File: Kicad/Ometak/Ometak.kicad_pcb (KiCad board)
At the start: 2 copper layers, 49.3 x 41 mm, 24 parts, among them J1 Conn_01x02_Pin, J2 Conn_01x02_Pin, J3 Conn_01x02_Pin, Q1 IRF7303, U1 L7805, U2 PIC16F15214-I/SN, U3 LM358

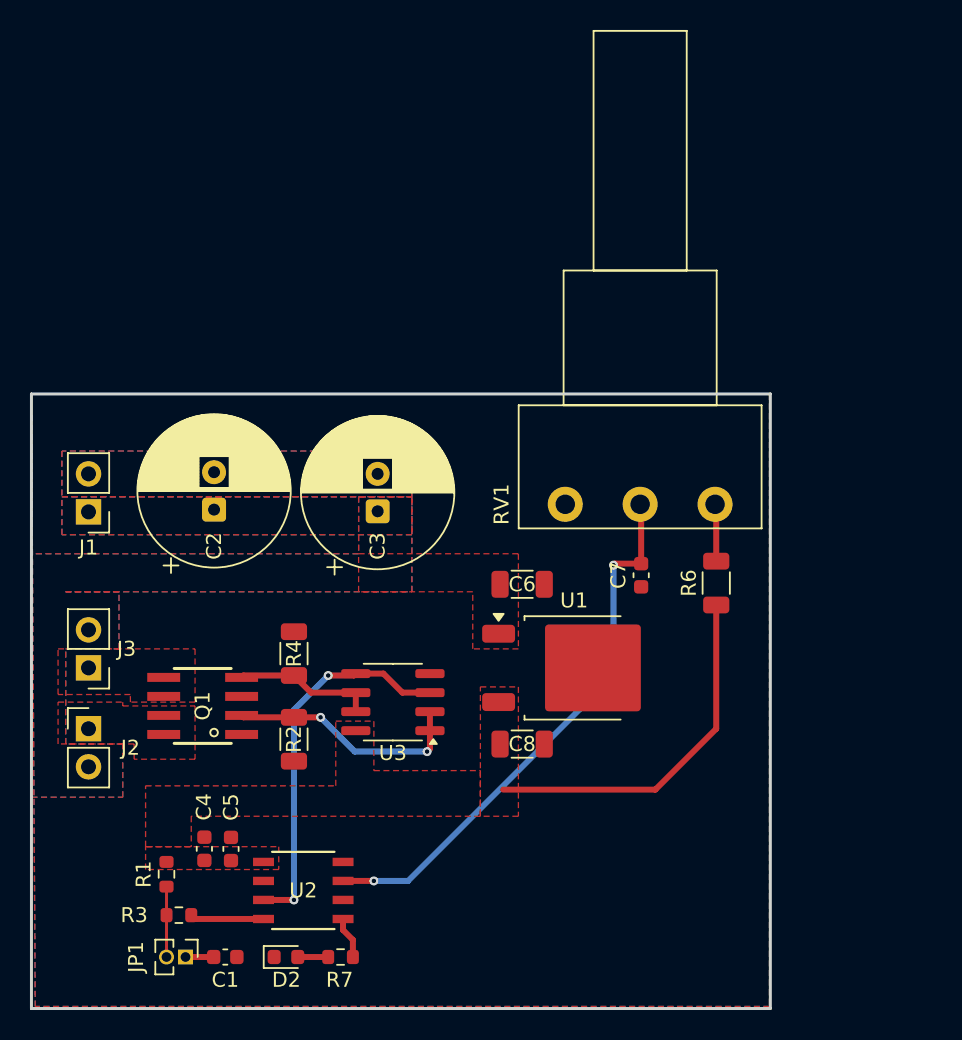
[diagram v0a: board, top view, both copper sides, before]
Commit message: Pokrocilejsi verze ometaku - navrh
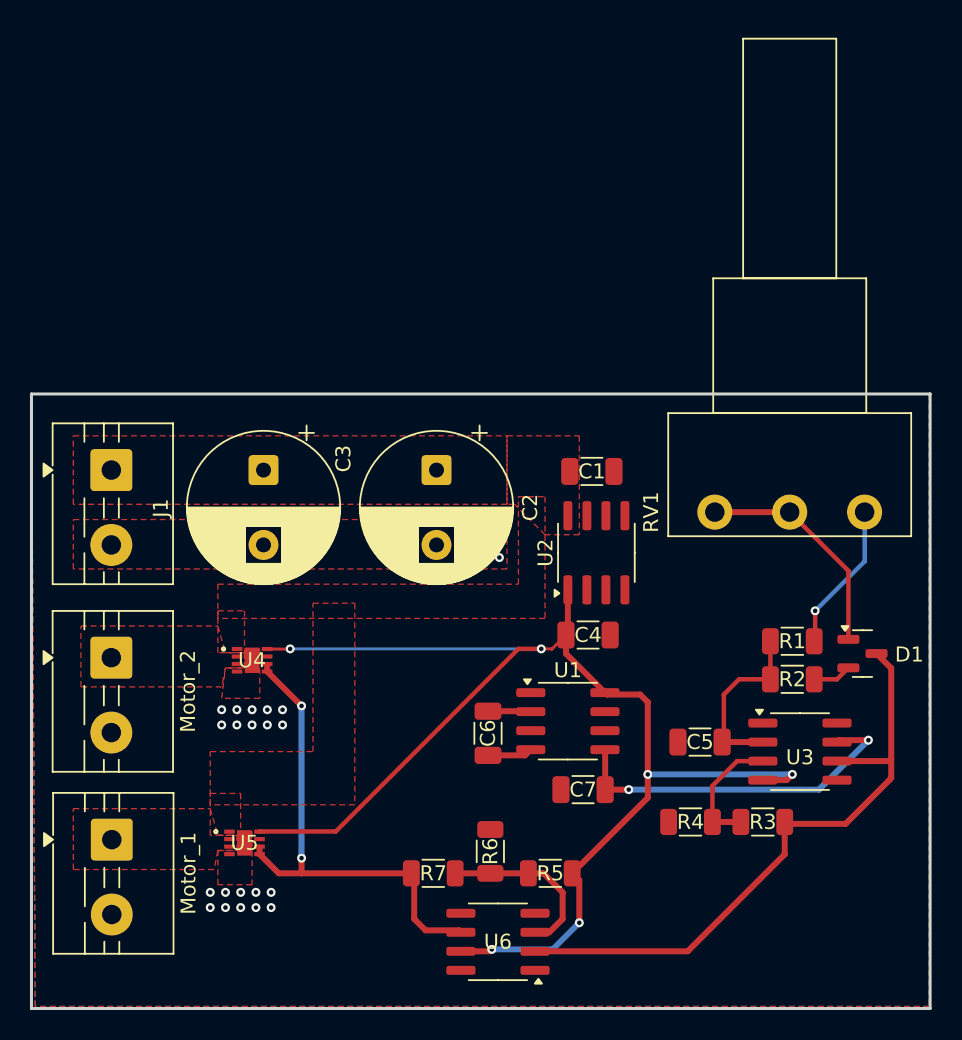
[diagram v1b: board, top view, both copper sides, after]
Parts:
- removed C8: 0.1u, Capacitor_SMD:C_1206_3216Metric
- removed D2: LED, LED_SMD:LED_0603_1608Metric
- removed J2, J3: Conn_01x02_Pin, Connector_PinHeader_2.54mm:PinHeader_1x02_P2.54mm_Vertical
- removed JP1: Jumper_2_Open, Connector_PinHeader_1.27mm:PinHeader_1x02_P1.27mm_Vertical
- removed Q1: IRF7303, IRF7303:SOIC-8
- added D1: BAS40-04, Package_TO_SOT_SMD:SOT-23, F.Cu at (132.4, 89.5)
- added Motor_1: Conn_01x02_Pin, TerminalBlock:TerminalBlock_MaiXu_MX126-5.0-02P_1x02_P5.00mm, F.Cu at (82.3, 101.9)
- added Motor_2: Conn_01x02_Pin, TerminalBlock:TerminalBlock_MaiXu_MX126-5.0-02P_1x02_P5.00mm, F.Cu at (82.3, 89.7)
- added R5: R, Resistor_SMD:R_1206_3216Metric, F.Cu at (111.6, 104.1)
- added U4: DRV8220DSGR, DRV8220:WSON8_DSG_TEX, F.Cu at (91.7, 89.9)
- added U5: DRV8220DSGR, DRV8220:WSON8_DSG_TEX, F.Cu at (91.2, 102.1)
- added U6: OPA333xxD, Package_SO:SOIC-8_3.9x4.9mm_P1.27mm, F.Cu at (108.1, 108.7)
- C1: value C -> 0.33 uF; footprint Capacitor_SMD:C_0603_1608Metric -> Capacitor_SMD:C_1206_3216Metric
- C2, C3: footprint Capacitor_THT:CP_Radial_D10.0mm_P2.50mm -> Capacitor_THT:CP_Radial_D10.0mm_P5.00mm
- C4: value C -> 0.1 uF; footprint Capacitor_SMD:C_0603_1608Metric -> Capacitor_SMD:C_1206_3216Metric
- C5: footprint Capacitor_SMD:C_0603_1608Metric -> Capacitor_SMD:C_1206_3216Metric
- C6: value 0.33u -> 10 uF
- C7: value C -> 10 uF; footprint Capacitor_SMD:C_0603_1608Metric -> Capacitor_SMD:C_1206_3216Metric
- J1: footprint Connector_PinHeader_2.54mm:PinHeader_1x02_P2.54mm_Vertical -> TerminalBlock:TerminalBlock_MaiXu_MX126-5.0-02P_1x02_P5.00mm
- R1: value R -> 25; footprint Resistor_SMD:R_0603_1608Metric -> Resistor_SMD:R_1206_3216Metric
- R3, R7: footprint Resistor_SMD:R_0603_1608Metric -> Resistor_SMD:R_1206_3216Metric
- U1: value L7805 -> ICL7660; footprint Package_TO_SOT_SMD:TO-252-2 -> Package_SO:SOIC-8_3.9x4.9mm_P1.27mm
- U2: value PIC16F15214-I/SN -> L78L05_SO8; footprint PIC16F15214:SOIC8_SN_MCH -> Package_SO:SOIC-8_3.9x4.9mm_P1.27mm
- U3: value LM358 -> OPA333xxD
- moved R1 44.6 mm to (127.8, 88.6), turned to 180 degrees
- moved C1 40.6 mm to (114.4, 77.3)
- moved R3 39.5 mm to (125.8, 100.7), turned to 180 degrees
- moved R2 33.5 mm to (127.8, 91.2), turned to 180 degrees
- moved C5 32.1 mm to (121.6, 95.4), turned to 180 degrees
- moved U2 29.9 mm to (114.7, 82.7), turned to 90 degrees
- moved C4 29.3 mm to (114.1, 88.2), turned to 0 degrees
- moved R4 28.8 mm to (121.0, 100.7), turned to 180 degrees
- moved U3 27.4 mm to (128.3, 96.0), turned to 0 degrees
- moved R6 23.4 mm to (107.6, 102.7)
- moved C2 15.1 mm to (104.0, 77.2), turned to -90 degrees
- moved C7 14.8 mm to (113.8, 98.6), turned to 0 degrees
- moved C6 10.2 mm to (107.4, 94.8), turned to -90 degrees
- moved RV1 10.00 mm to (132.6, 80.0)
- moved R7 8.34 mm to (103.8, 104.1)
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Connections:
- C1 pad 1: Net-(JP1-A) -> V+_SUPPLY
- C2 pad 1: +12V -> V+_SUPPLY
- C3 pad 1: +12V -> V+_SUPPLY
- C4 pad 1: +5V -> VIN+
- C5 pad 1: +5V -> Net-(U3--)
- C6 pad 1: +12V -> Net-(U1-CAP+)
- C6 pad 2: GND -> Net-(U1-CAP-)
- C7 pad 1: ADC_POT -> GND
- C7 pad 2: GND -> VIN-
- J1 pad 1: +12V -> V+_SUPPLY
- R1 pad 1: +5V -> Net-(R1-Pad1)
- R1 pad 2: Net-(JP1-B) -> Net-(U3--)
- R2 pad 1: GND -> Net-(D1-Pad2)
- R2 pad 2: Net-(U3A--) -> Net-(U3--)
- R3 pad 1: Net-(JP1-B) -> Net-(U6--)
- R3 pad 2: MCLR -> Net-(U3-+)
- R4 pad 1: GND -> Net-(U3-+)
- R4 pad 2: Net-(U3B--) -> GND
- R6 pad 1: +5V -> Net-(U6-+)
- R6 pad 2: Net-(R6-Pad2) -> GND
- R7 pad 1: LED -> Net-(U6-+)
- R7 pad 2: Net-(D2-A) -> SQUARE_OUT
- RV1 pad 1: Net-(R6-Pad2) -> Net-(R1-Pad1)
- RV1 pad 2: ADC_POT -> Net-(D1-Pad1)
- RV1 pad 3: GND -> Net-(D1-Pad1)
- U1 pad 1: +12V -> unconnected-(U1-NC-Pad1)
- U1 pad 2: GND -> Net-(U1-CAP+)
- U1 pad 3: +5V -> GND
- U2 pad 1: +5V -> VIN+
- U2 pad 2: unconnected-(U2-RA5-Pad2) -> GND
- U2 pad 3: PWM_Motor -> GND
- U2 pad 4: MCLR -> unconnected-(U2-NC-Pad4)
- U2 pad 5: LED -> unconnected-(U2-NC-Pad5)
- U2 pad 6: ADC_Motor -> GND
- U2 pad 7: ADC_POT -> GND
- U2 pad 8: GND -> V+_SUPPLY
- U3 pad 1: Net-(U3A--) -> unconnected-(U3-NC-Pad1)
- U3 pad 2: Net-(U3A--) -> Net-(U3--)
- U3 pad 3: PWM_Motor -> Net-(U3-+)
- U3 pad 4: GND -> VIN+
- U3 pad 5: PWM_Motor -> unconnected-(U3-NC-Pad5)
- U3 pad 6: Net-(U3B--) -> Net-(U6--)
- U3 pad 7: Net-(U3B--) -> VIN-
- U3 pad 8: +5V -> unconnected-(U3-NC-Pad8)
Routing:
- net VIN+: track 0.00 -> 92.8 mm, vias 0 -> 6
- net Net-(U6--): track 0.00 -> 42.3 mm
- net ADC_POT: track 37.0 -> 0.00 mm, vias 2 -> 0
- net SQUARE_OUT: track 0.00 -> 32.6 mm, vias 0 -> 2
- net PWM_Motor: track 25.3 -> 0.00 mm, vias 2 -> 0
- net +5V: track 24.2 -> 0.00 mm
- net VIN-: track 0.00 -> 23.8 mm, vias 0 -> 2
- net Net-(U3A--): track 16.1 -> 0.00 mm, vias 2 -> 0
- net Net-(D1-Pad1): track 0.00 -> 15.1 mm
- net Net-(U3--): track 0.00 -> 12.0 mm
- net Net-(U6-+): track 0.00 -> 11.7 mm
- net Net-(R1-Pad1): track 0.00 -> 10.0 mm, vias 0 -> 1
- net Net-(U3B--): track 9.42 -> 0.00 mm
- net Net-(U3-+): track 0.00 -> 8.36 mm
- net MCLR: track 4.93 -> 0.00 mm
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- added copper zone on F.Cu, net Motor_1+
- added copper zone on F.Cu, net Motor_2+
- added copper zone on F.Cu, net V+_SUPPLY
- removed copper zone on B.Cu, net +12V
- removed copper zone on F.Cu, net +12V
- removed copper zone on F.Cu, net +5V
- removed copper zone on F.Cu, net MOT_A
- removed copper zone on F.Cu, net MOT_B
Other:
- board size 49.3 x 41 mm -> 60 x 41 mm
